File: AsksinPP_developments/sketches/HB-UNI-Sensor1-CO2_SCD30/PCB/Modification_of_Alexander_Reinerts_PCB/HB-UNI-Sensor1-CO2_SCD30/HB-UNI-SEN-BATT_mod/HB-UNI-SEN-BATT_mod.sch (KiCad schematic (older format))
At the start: 35 parts, among them J10 Conn_01x02-conn, J11 Conn_01x04-conn, J12 Conn_01x04-conn, J13 Conn_01x04-conn, J14 Conn_01x04-conn, J4 Conn_01x02-conn, J5 GS2-conn, J6 Conn_01x04-conn, J7 Conn_01x02-conn, J8 Conn_01x02-conn, J9 Conn_01x02-conn, Q1 BC327, SW2 SW_DIP_x01-switches, U1 CC1101-RESCUE-HB-UNI-SEN-BATT, U2 ArduinoProMini

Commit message: fixes and doc updates
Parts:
- added R12, R13, R14: 47k, symbol Device:R
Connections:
- wire segments 185 -> 191
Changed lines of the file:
@@
 	3650 5250 3950 5250
-Wire Wire Line
-	3650 5350 3950 5350
-Wire Wire Line
-	3650 5450 3950 5450
 Wire Wire Line
 	3650 5550 3950 5550
@@
 Text Notes 6150 2800 0    50   ~ 0
 VCC depends on source of power supply:\na) Step-Up converter Module4:   3.7V\nb) 6V DC input power supply and Step-Down converter: 3.8V\nc) Solar suppy and Step-Up converter: 3.7 .. 3.9V (depends on sun light intensity)
-Text Notes 4150 5200 0    50   ~ 10
+Text Notes 900  4950 0    50   ~ 10
 For power saving, please desolder\nvoltage regulator and red LED from\nArduino Pro Mini module
 NoConn ~ 3650 4150
@@
 Text Notes 8100 1200 0    50   ~ 0
 A 470 uF decoupling capacitor attached to the I2C sockets has been removed !
+$Comp
+L Device:R R12
+U 1 1 6015794F
+P 4200 5450
+F 0 "R12" V 4300 5450 50  0000 C CNN
+F 1 "47k" V 4200 5450 50  0000 C CNN
+F 2 "" V 4130 5450 50  0001 C CNN
+F 3 "~" H 4200 5450 50  0001 C CNN
+	1    4200 5450
+	0    1    1    0
+$EndComp
+$Comp
+L Device:R R14
+U 1 1 601625EB
+P 4350 5100
+F 0 "R14" H 4420 5146 50  0000 L CNN
+F 1 "47k" H 4420 5055 50  0000 L CNN
+F 2 "" V 4280 5100 50  0001 C CNN
+F 3 "~" H 4350 5100 50  0001 C CNN
+	1    4350 5100
+	1    0    0    -1
+$EndComp
+$Comp
+L Device:R R13
+U 1 1 60162E56
+P 4350 4750
+F 0 "R13" H 4420 4796 50  0000 L CNN
+F 1 "47k" H 4420 4705 50  0000 L CNN
+F 2 "" V 4280 4750 50  0001 C CNN
+F 3 "~" H 4350 4750 50  0001 C CNN
+	1    4350 4750
+	1    0    0    -1
+$EndComp
+Wire Wire Line
+	3650 5450 4050 5450
+Wire Wire Line
+	4350 5450 4350 5350
+Wire Wire Line
+	4350 4950 4350 4900
+Wire Wire Line
+	4350 4600 4350 3450
+Wire Wire Line
+	4350 3450 2600 3450
+Wire Wire Line
+	2600 3450 2600 2450
+Wire Wire Line
+	3650 5350 4350 5350
+Connection ~ 4350 5350
+Wire Wire Line
+	4350 5350 4350 5250
 $EndSCHEMATC

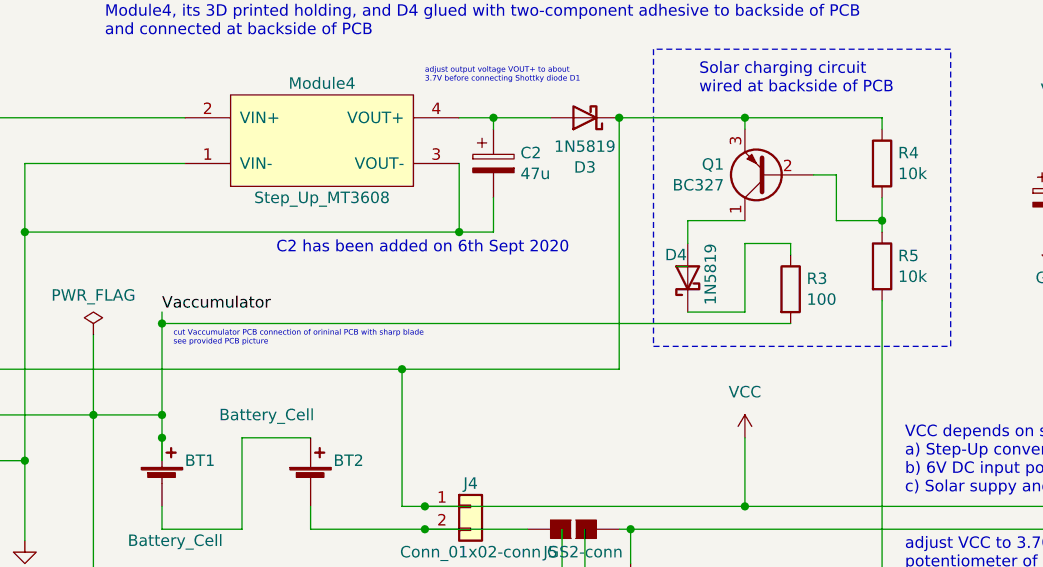
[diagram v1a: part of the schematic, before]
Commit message: HB-UNI-Sensor1-AQ-BME680_KF, HB-UNI-Sensor1-AQ-BME680_KF_DEBUG: improved concergence; HB-UNI-Sensor1-CO2_SCD30: updated schematics
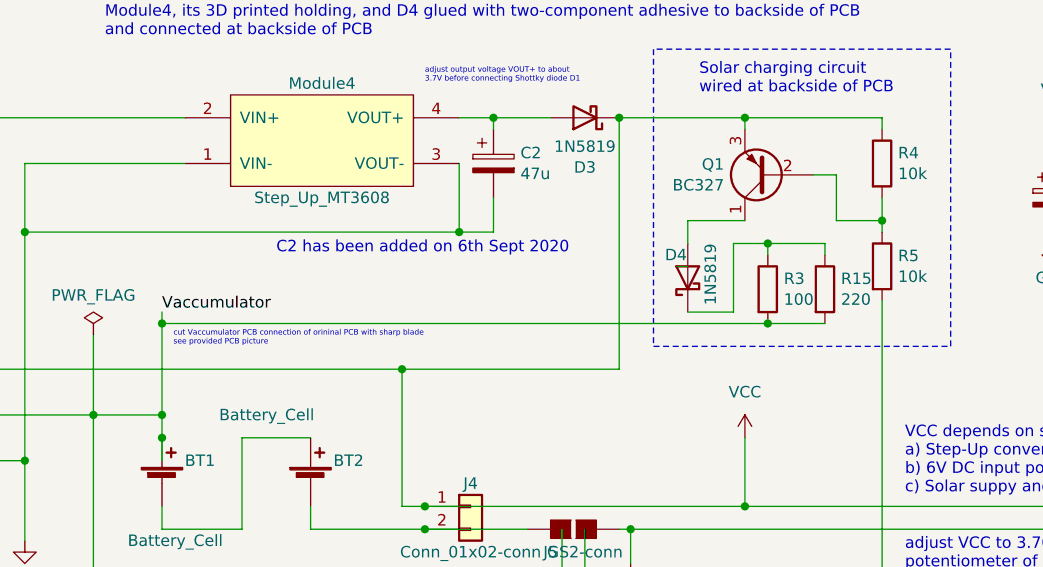
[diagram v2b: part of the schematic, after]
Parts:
- added R15: 220, symbol Device:R
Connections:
- wire segments 191 -> 194
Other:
- moved on the sheet: R3
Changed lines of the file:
@@
 L Device:R R3
 U 1 1 5F4DDD7A
-P 5650 1900
-F 0 "R3" H 5720 1946 50  0000 L CNN
-F 1 "100" H 5720 1855 50  0000 L CNN
-F 2 "" V 5580 1900 50  0001 C CNN
-F 3 "~" H 5650 1900 50  0001 C CNN
-	1    5650 1900
+P 5550 1900
+F 0 "R3" H 5620 1946 50  0000 L CNN
+F 1 "100" H 5620 1855 50  0000 L CNN
+F 2 "" V 5480 1900 50  0001 C CNN
+F 3 "~" H 5550 1900 50  0001 C CNN
+	1    5550 1900
 	1    0    0    -1
 $EndComp
@@
 	5200 1800 5150 1800
 Wire Wire Line
-	2900 2050 5650 2050
-Wire Wire Line
-	5650 1750 5650 1700
-Wire Wire Line
-	5650 1700 5450 1700
-Wire Wire Line
-	5450 1700 5450 2000
-Wire Wire Line
-	5450 2000 5200 2000
+	2900 2050 5550 2050
+Wire Wire Line
+	5550 1750 5550 1700
+Wire Wire Line
+	5400 1700 5400 2000
+Wire Wire Line
+	5400 2000 5200 2000
 Wire Wire Line
 	5200 1700 5200 1600
@@
 Wire Wire Line
 	4350 5350 4350 5250
+$Comp
+L Device:R R15
+U 1 1 60D1AD6E
+P 5800 1900
+F 0 "R15" H 5870 1946 50  0000 L CNN
+F 1 "220" H 5870 1855 50  0000 L CNN
+F 2 "" V 5730 1900 50  0001 C CNN
+F 3 "~" H 5800 1900 50  0001 C CNN
+	1    5800 1900
+	1    0    0    -1
+$EndComp
+Wire Wire Line
+	5800 1750 5800 1700
+Wire Wire Line
+	5800 1700 5550 1700
+Connection ~ 5550 1700
+Wire Wire Line
+	5800 2050 5550 2050
+Connection ~ 5550 2050
+Wire Wire Line
+	5400 1700 5550 1700
 $EndSCHEMATC
